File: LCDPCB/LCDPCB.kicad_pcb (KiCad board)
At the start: 2 copper layers, 60 x 64 mm, 32 parts, among them J1 Sockets, J2 Hot Plug, J3 Programming Header, J4 Conn_01x08_Male, J5 Conn_01x08_Male, SW1 SW_Push, U1 STM32F091RCT6, U2 LD1117S12TR_SOT223

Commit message: added logo
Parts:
- added G***: LOGO, LOGO, F.Cu at (126.1, 70.6)
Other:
- board text added: "NYAKB: Not Your Average Keyboard Sub-module ECE 477: Team 3 Anna Shen Connor Chadwick Avanish Subbiah Jackson Moffet"

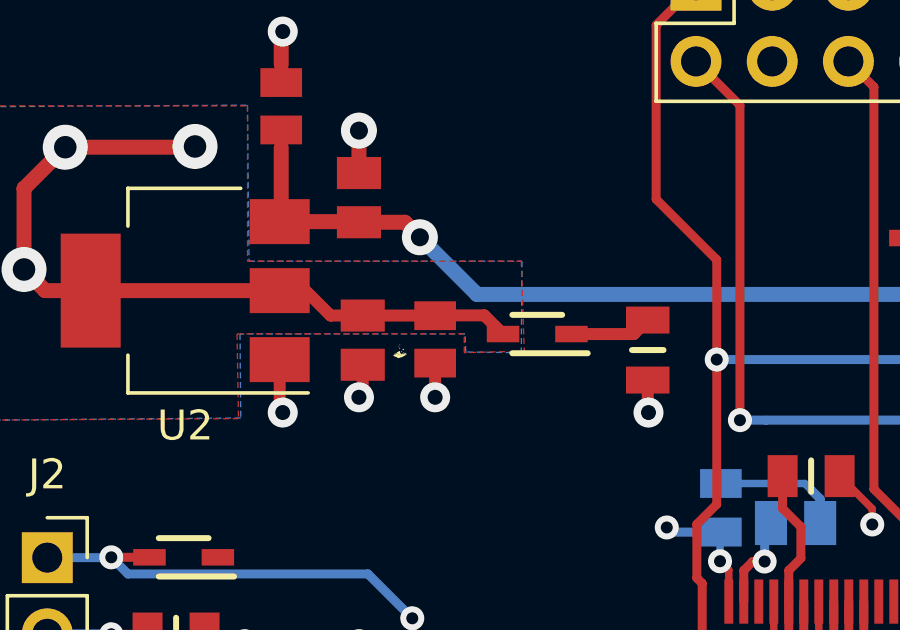
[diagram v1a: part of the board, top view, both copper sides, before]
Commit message: added drill to gerber
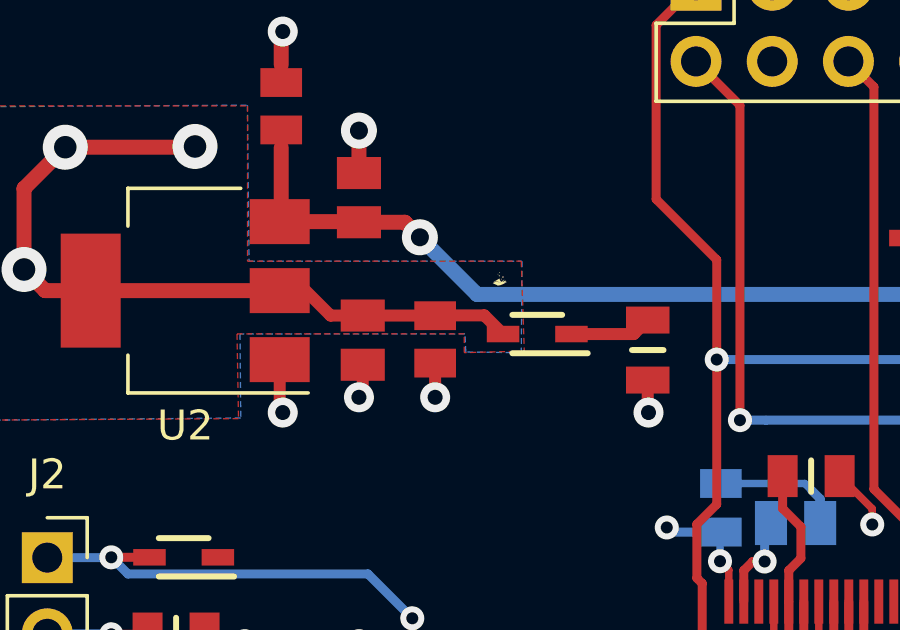
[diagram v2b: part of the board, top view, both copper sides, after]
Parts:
- moved G*** 4.11 mm to (129.4, 68.2)
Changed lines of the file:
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@@
       (viasonmask true)
       (mode 1)
-      (useauxorigin false)
+      (useauxorigin true)
       (hpglpennumber 1)
       (hpglpenspeed 20)
@@
   )
   (footprint "LOGO" (layer "F.Cu")
-    (at 126.0856 70.612)
+    (at 129.413 68.199)
     (attr board_only exclude_from_pos_files exclude_from_bom)
     (fp_text reference "G***" (at 0 0) (layer "F.SilkS") hide

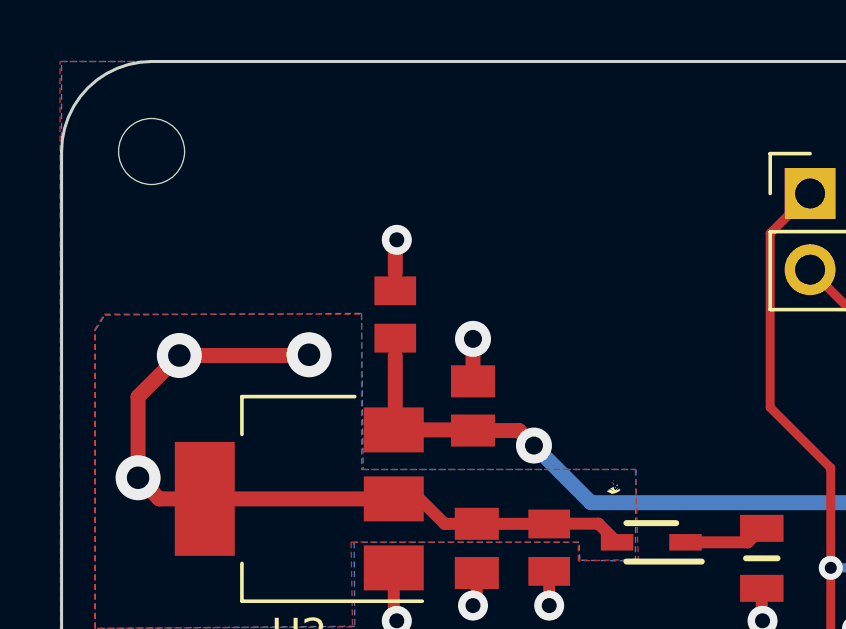
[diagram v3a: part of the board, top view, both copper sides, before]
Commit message: renamed pa13 and 14
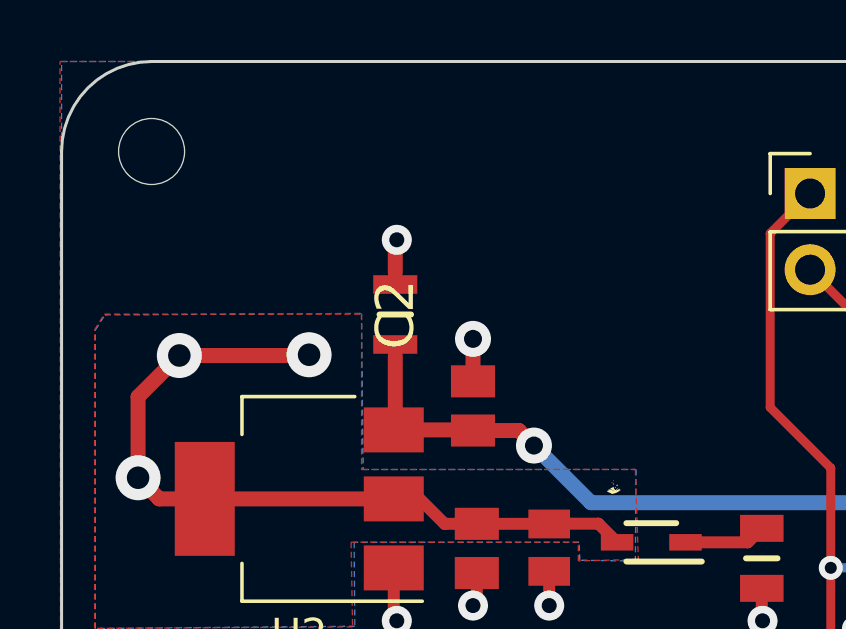
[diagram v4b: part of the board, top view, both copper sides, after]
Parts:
- C2: footprint lib_file:10uF -> lib_file:new10uf
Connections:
- J3 pad 2: PA13 -> /SWDIO_IN
- J3 pad 6: PA14 -> /SWCLK_IN
- U1 pad 46: PA13 -> /SWDIO_IN
- U1 pad 49: PA14 -> /SWCLK_IN
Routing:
- net PA13: track 77.6 -> 0.00 mm, vias 6 -> 0
- net /SWDIO_IN: track 0.00 -> 77.6 mm, vias 0 -> 6
- net PA14: track 74.6 -> 0.00 mm, vias 5 -> 0
- net /SWCLK_IN: track 0.00 -> 74.6 mm, vias 0 -> 5
